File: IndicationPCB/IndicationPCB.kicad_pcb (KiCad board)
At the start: 2 copper layers, 14 x 32 mm, 6 parts, among them J1 Conn_01x03

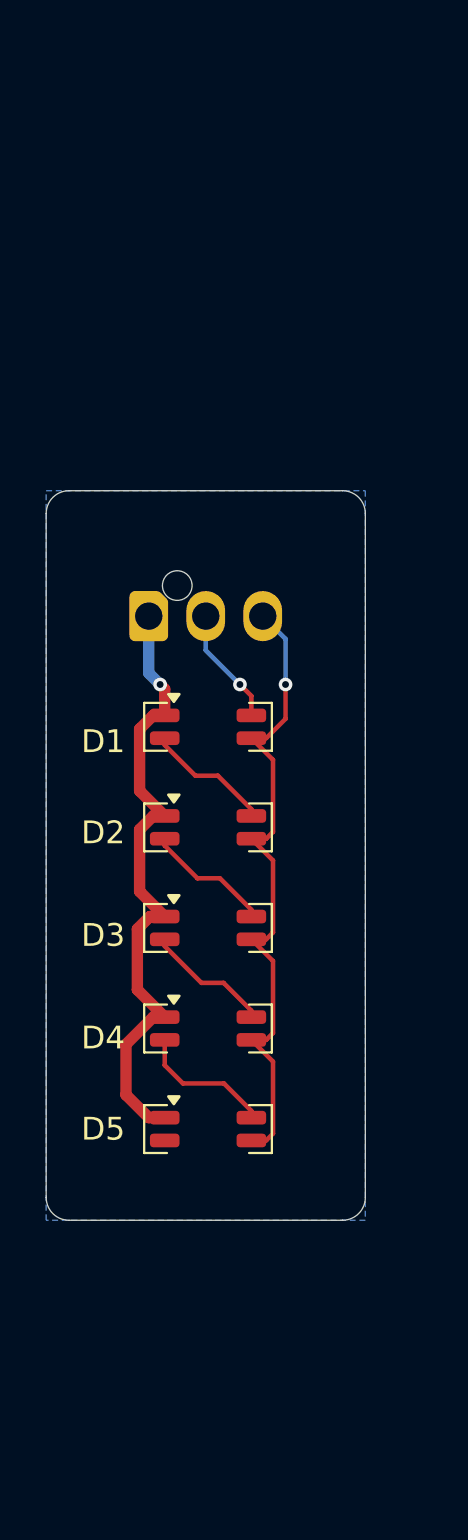
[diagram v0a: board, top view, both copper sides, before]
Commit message: correct LEDS
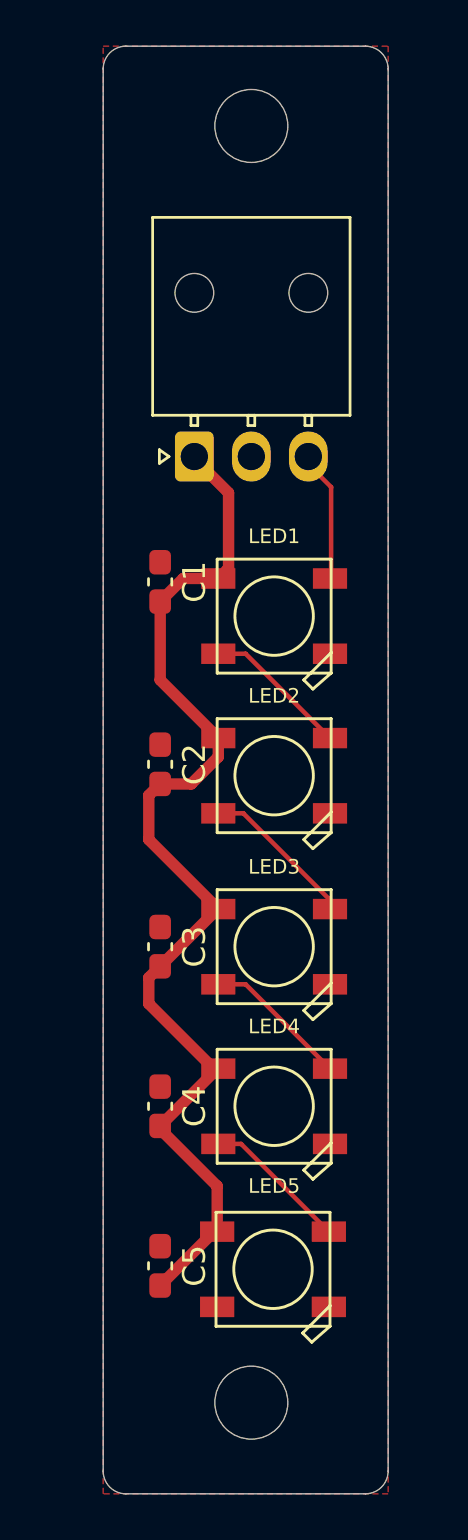
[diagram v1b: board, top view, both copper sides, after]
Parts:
- removed D1, D2, D3, D4, D5: LTST-C235KGKRKT, LED_SMD:LED_LiteOn_LTST-C235KGKRKT
- added C1: 1uF, Capacitor_SMD:C_0603_1608Metric_Pad1.08x0.95mm_HandSolder, F.Cu at (140.0, 72.0)
- added C2: 1uF, Capacitor_SMD:C_0603_1608Metric_Pad1.08x0.95mm_HandSolder, F.Cu at (140.0, 80.0)
- added C3: 1uF, Capacitor_SMD:C_0603_1608Metric_Pad1.08x0.95mm_HandSolder, F.Cu at (140.0, 88.0)
- added C4: 1 uF, Capacitor_SMD:C_0603_1608Metric_Pad1.08x0.95mm_HandSolder, F.Cu at (140.0, 95.0)
- added C5: 1uF, Capacitor_SMD:C_0603_1608Metric_Pad1.08x0.95mm_HandSolder, F.Cu at (140.0, 102.0)
- added H1: MountingHole, MountingHole:MountingHole_3.2mm_M3, F.Cu at (144.0, 52.0)
- added H2: MountingHole, MountingHole:MountingHole_3.2mm_M3, F.Cu at (144.0, 108.0)
- added LED1: WS2812B, WS2812B:WS2812B, F.Cu at (145.0, 73.5)
- added LED2: WS2812B, WS2812B:WS2812B, F.Cu at (145.0, 80.5)
- added LED3: WS2812B, WS2812B:WS2812B, F.Cu at (145.0, 88.0)
- added LED4: WS2812B, WS2812B:WS2812B, F.Cu at (145.0, 95.0)
- added LED5: WS2812B, WS2812B:WS2812B, F.Cu at (144.9, 102.2)
- J1: footprint Connector_Molex:Molex_Nano-Fit_105309-xx03_1x03_P2.50mm_Vertical -> Connector_Molex:Molex_Nano-Fit_105313-xx03_1x03_P2.50mm_Horizontal; moved to F.Cu
- moved J1 7.28 mm to (141.5, 66.5), turned to 90 degrees
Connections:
- J1 pad 2: Net-(D1-A2) -> GND
- J1 pad 3: GND -> /DIN
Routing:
- net GND: track 29.1 -> 0.00 mm, vias 1 -> 0
- net +5V: track 28.2 -> 49.0 mm, vias 1 -> 0
- net Net-(LED2-DO): track 0.00 -> 6.87 mm
- net Net-(LED4-DO): track 0.00 -> 6.44 mm
- net Net-(LED3-DO): track 0.00 -> 6.43 mm
- net Net-(LED1-DO): track 0.00 -> 6.43 mm
- net Net-(D4-K1): track 6.04 -> 0.00 mm
- net Net-(D2-K1): track 5.56 -> 0.00 mm
- net Net-(D1-K1): track 5.56 -> 0.00 mm
- net Net-(D3-K1): track 5.56 -> 0.00 mm
- net /DIN: track 0.00 -> 5.44 mm
- net Net-(D1-A2): track 5.18 -> 0.00 mm, vias 1 -> 0
- added copper zone on F.Cu, net GND
- removed copper zone on B.Cu, net GND
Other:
- board size 14 x 32 mm -> 12.5 x 63.5 mm

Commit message: Added Models
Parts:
- added LOGO1: Dr. Hallock, UTSVT_Logos:UTSVT_Logo_Symbol, B.Cu at (144.0, 80.5)
- moved J1 7.29 mm to (148.1, 63.5), turned to 180 degrees
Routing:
- net /DIN: track 5.44 -> 14.8 mm
- net +5V: track 49.0 -> 53.9 mm
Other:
- board text added: "2025"
- board text added: "G"
- board text added: "Indication PCB"

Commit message: fixed
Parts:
- moved H1 0.50 mm to (144.5, 52.0)
- moved H2 0.50 mm to (144.5, 108.0)
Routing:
- net /DIN: track 14.8 -> 16.4 mm
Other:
- board size 12.5 x 63.5 mm -> 14.5 x 63 mm
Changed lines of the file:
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@@
 	(footprint "MountingHole:MountingHole_3.2mm_M3"
 		(layer "F.Cu")
-		(at 144 52)
+		(at 144.5 52)
 		(descr "Mounting Hole 3.2mm, no annular, M3")
 		(tags "mounting hole 3.2mm no annular m3")
@@
 	(footprint "MountingHole:MountingHole_3.2mm_M3"
 		(layer "F.Cu")
-		(at 144 108)
+		(at 144.5 108)
 		(descr "Mounting Hole 3.2mm, no annular, M3")
 		(tags "mounting hole 3.2mm no annular m3")
@@
 		(embedded_fonts no)
 	)
-	(gr_arc
-		(start 138.5 112)
-		(mid 137.792893 111.707107)
-		(end 137.5 111)
+	(gr_rect
+		(start 137 48.5)
+		(end 151.5 111.5)
 		(stroke
 			(width 0.05)
 			(type default)
 		)
-		(layer "Edge.Cuts")
-	)
-	(gr_arc
-		(start 149 48.5)
-		(mid 149.707107 48.792893)
-		(end 150 49.5)
-		(stroke
-			(width 0.05)
-			(type default)
-		)
-		(layer "Edge.Cuts")
-	)
-	(gr_line
-		(start 137.5 111)
-		(end 137.5 49.5)
-		(stroke
-			(width 0.05)
-			(type default)
-		)
-		(layer "Edge.Cuts")
-	)
-	(gr_line
-		(start 150 49.5)
-		(end 150 111)
-		(stroke
-			(width 0.05)
-			(type default)
-		)
-		(layer "Edge.Cuts")
-	)
-	(gr_line
-		(start 138.5 48.5)
-		(end 149 48.5)
-		(stroke
-			(width 0.05)
-			(type default)
-		)
-		(layer "Edge.Cuts")
-	)
-	(gr_line
-		(start 149 112)
-		(end 138.5 112)
-		(stroke
-			(width 0.05)
-			(type default)
-		)
-		(layer "Edge.Cuts")
-	)
-	(gr_arc
-		(start 137.5 49.5)
-		(mid 137.792893 48.792893)
-		(end 138.5 48.5)
-		(stroke
-			(width 0.05)
-			(type default)
-		)
-		(layer "Edge.Cuts")
-	)
-	(gr_arc
-		(start 150 111)
-		(mid 149.707107 111.707107)
-		(end 149 112)
-		(stroke
-			(width 0.05)
-			(type default)
-		)
+		(fill no)
 		(layer "Edge.Cuts")
 	)
@@
 	(segment
 		(start 147.45 71.85)
-		(end 149.541 69.759)
+		(end 150.899 68.401)
 		(width 0.2)
 		(layer "F.Cu")
@@
 	)
 	(segment
-		(start 149.541 69.759)
-		(end 149.541 59.901)
+		(start 150.899 60.399)
+		(end 149 58.5)
 		(width 0.2)
 		(layer "F.Cu")
@@
 	)
 	(segment
-		(start 149.541 59.901)
+		(start 149 58.5)
 		(end 148.14 58.5)
+		(width 0.2)
+		(layer "F.Cu")
+		(net 3)
+	)
+	(segment
+		(start 150.899 68.401)
+		(end 150.899 60.399)
 		(width 0.2)
 		(layer "F.Cu")
@@
 		(polygon
 			(pts
-				(xy 137.5 48.5) (xy 150 48.5) (xy 150 112) (xy 137.5 112)
-			)
-		)
+				(xy 137 48.5) (xy 151.5 48.5) (xy 151.5 111.5) (xy 137 111.5)
+			)
+		)
